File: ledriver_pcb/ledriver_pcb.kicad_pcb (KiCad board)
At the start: 2 copper layers, 83.8 x 73.7 mm, 43 parts, among them J1 5-12vdc, J10 POT2, J11 I2C, J12 Serial2, J13 Serial1, J14 M3, J15 M3, J16 M3, J17 M3, J2 USB_B, J3 USB+-, J4 USB_EXT, J5 RJ2, J6 CONN-114-00841-68-MICROSD, J7 RJ1, J8 led_out_clk, J9 POT1, SW1 SW_SPST, SW2 SW_SPST, SW3 SW_SPST, U1 L7805, U2 MCP1825, U3 WIZ820IO, U4 74HC245, U5 Teensy3.2

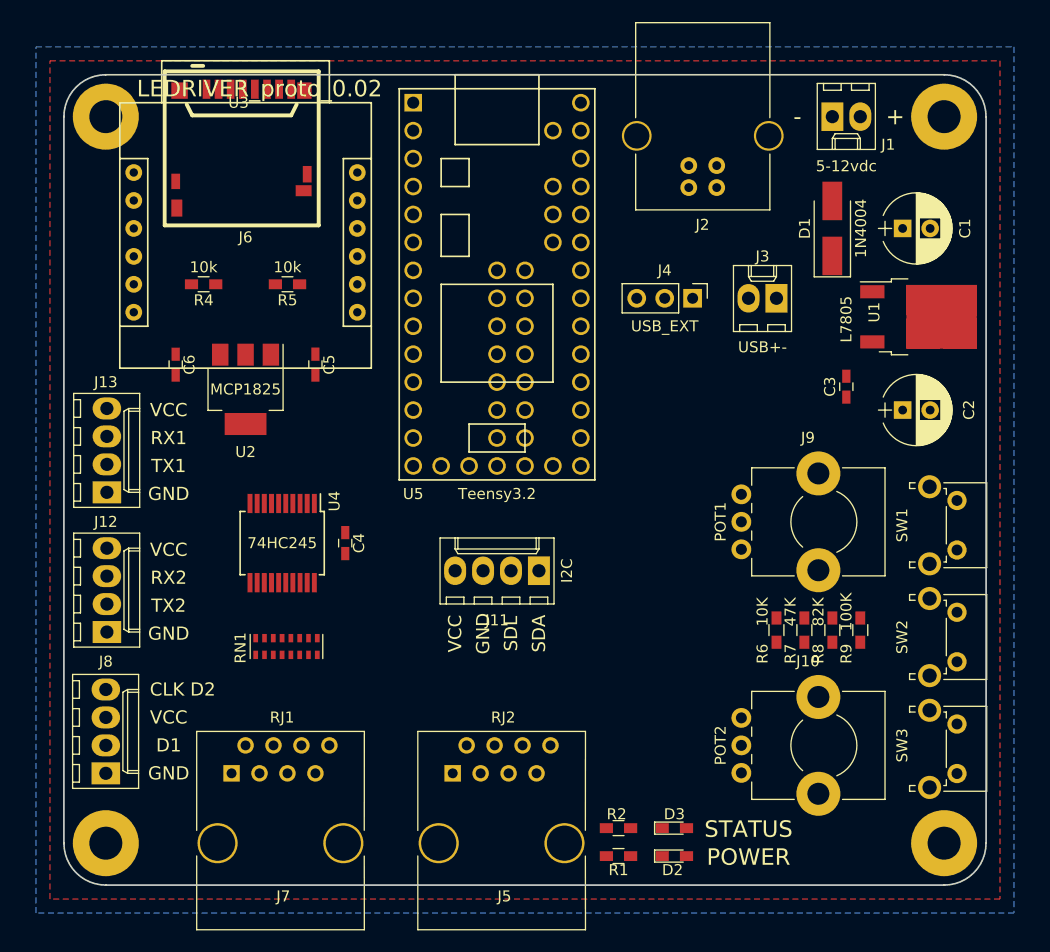
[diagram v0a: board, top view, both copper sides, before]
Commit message: changed led SPI output to use pin 7 and 14, not reflected in layout
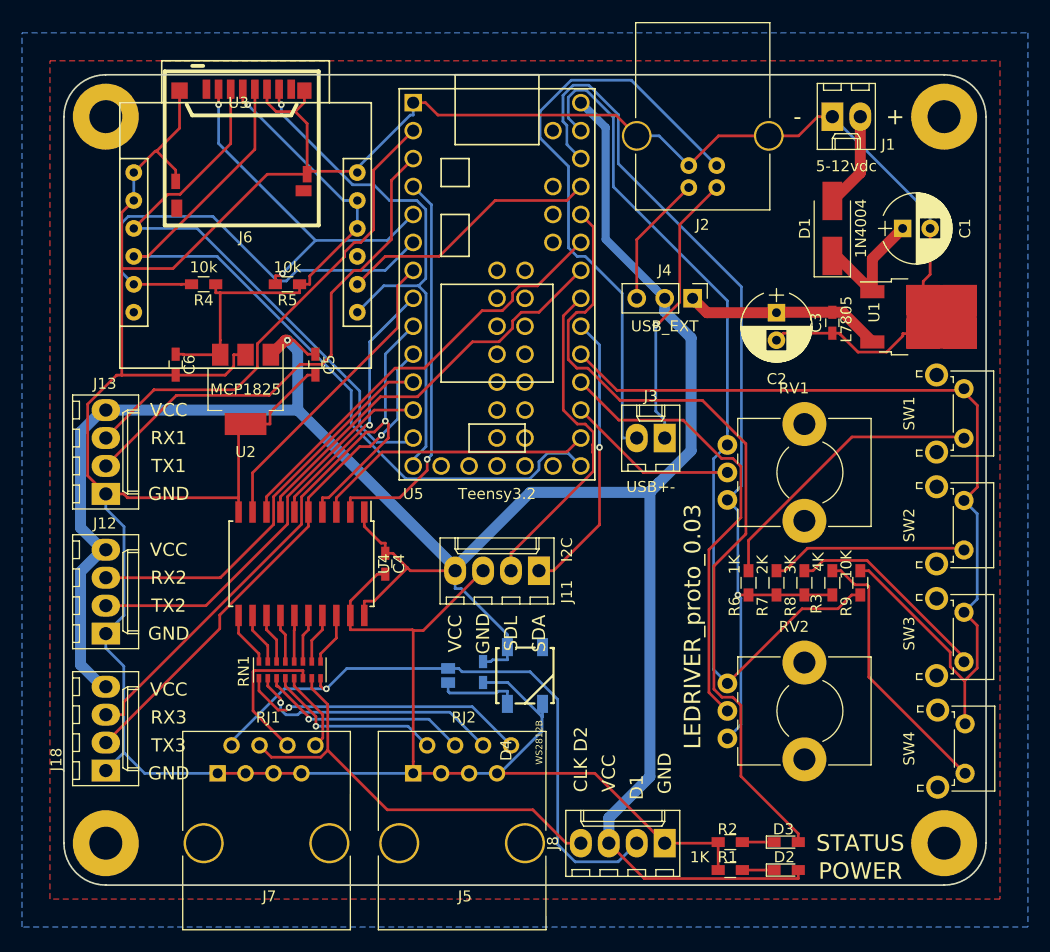
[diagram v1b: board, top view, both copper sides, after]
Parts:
- removed J10: POT2, Potentiometers:Potentiometer_Bourns_PTV09A-1_Horizontal
- removed J9: POT1, Potentiometers:Potentiometer_Bourns_PTV09A-1_Horizontal
- added C7: C, Capacitors_SMD:C_0603_HandSoldering, B.Cu at (138.4, 88.6)
- added D4: WS2812B, SparkFun-LED:WS2812B, B.Cu at (142.2, 88.9)
- added J18: Serial3, Connectors_Molex:Molex_KK-6410-04_04x2.54mm_Straight, F.Cu at (104.1, 97.5)
- added J19: underglow, Connectors:GS2, B.Cu at (135.3, 88.9)
- added R3: 4K, Resistors_SMD:R_0603_HandSoldering, F.Cu at (170.2, 80.5)
- added RV1: POT, Potentiometers:Potentiometer_Bourns_PTV09A-1_Horizontal, F.Cu at (160.6, 72.9)
- added RV2: POT, Potentiometers:Potentiometer_Bourns_PTV09A-1_Horizontal, F.Cu at (160.6, 94.6)
- added SW4: SW_SPST, Buttons_Switches_THT:SW_Tactile_SPST_Angled_PTS645Vx39-2LFS, F.Cu at (182.2, 93.3)
- R6: value 10K -> 1K
- R7: value 47K -> 2K
- R8: value 82K -> 3K
- R9: value 100K -> 10K
- U4: footprint Housings_SSOP:SSOP-20_5.3x7.2mm_Pitch0.65mm -> Housings_SOIC:SOIC-20W_7.5x12.8mm_Pitch1.27mm
- moved J8 51.2 mm to (154.9, 104.1), turned to 180 degrees
- moved J3 16.3 mm to (154.9, 67.3)
- moved C2 14.5 mm to (165.1, 55.9), turned to 270 degrees
- moved D2 10.2 mm to (166.0, 106.6)
- moved D3 10.2 mm to (166.0, 104.0)
- moved R1 10.2 mm to (160.9, 106.6)
- moved R2 10.2 mm to (160.9, 104.0)
- moved SW2 10.2 mm to (182.1, 73.0)
- moved SW1 10.2 mm to (182.1, 62.8)
- moved SW3 10.2 mm to (182.1, 83.2)
- moved C3 5.95 mm to (170.2, 56.8)
- moved R8 4.99 mm to (167.6, 80.5)
- moved R6 4.99 mm to (162.6, 80.5)
- moved R7 4.99 mm to (165.1, 80.5)
- moved R9 4.30 mm to (172.7, 80.5)
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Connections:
- R6 pad 1: VCC -> +3V3
- R7 pad 1: VCC -> +3V3
- R8 pad 1: VCC -> +3V3
- R9 pad 1: GND -> GNDA
- U5 pad 31: (no net) -> +3V3
- U5 pad 32: (no net) -> GNDA
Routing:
- net GND: track 0.00 -> 357.4 mm
- net VCC: track 0.00 -> 225.8 mm, vias 0 -> 1
- net +3V3: track 0.00 -> 84.4 mm, vias 0 -> 1
- net /BUTTONS: track 0.00 -> 84.0 mm
- net GNDA: track 0.00 -> 81.1 mm
- net /STATUS: track 0.00 -> 75.5 mm
- net /SPI_SCK: track 0.00 -> 73.2 mm
- net /DATA_3_PIN_7: track 0.00 -> 59.5 mm, vias 0 -> 1
- net Net-(J19-Pad2): track 0.00 -> 57.0 mm, vias 0 -> 1
- net Net-(J2-Pad3): track 0.00 -> 55.0 mm
- net /SPI_DOUT: track 0.00 -> 52.4 mm
- net /SPI_DIN: track 0.00 -> 49.9 mm, vias 0 -> 1
- net /DATA_4_PIN_8: track 0.00 -> 47.4 mm, vias 0 -> 1
- net /TX1: track 0.00 -> 46.0 mm
- net Net-(C6-Pad1): track 0.00 -> 44.5 mm, vias 0 -> 1
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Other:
- board text added: "LEDRIVER_proto_0.03"
- board text added: "RX3"
- board text added: "TX3"
- board text removed: "LEDRIVER_proto_0.02"
- board text removed: "sdcard move up"

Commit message: hjaha
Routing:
- net GND: track 357.4 -> 0.00 mm
- net VCC: track 225.8 -> 0.00 mm, vias 1 -> 0
- net +3V3: track 84.4 -> 0.00 mm, vias 1 -> 0
- net /BUTTONS: track 84.0 -> 0.00 mm
- net GNDA: track 81.1 -> 0.00 mm
- net /STATUS: track 75.5 -> 0.00 mm
- net /SPI_SCK: track 73.2 -> 0.00 mm
- net /DATA_3_PIN_7: track 59.5 -> 0.00 mm, vias 1 -> 0
- net Net-(J19-Pad2): track 57.0 -> 0.00 mm, vias 1 -> 0
- net Net-(J2-Pad3): track 55.0 -> 0.00 mm
- net /SPI_DOUT: track 52.4 -> 0.00 mm
- net /SPI_DIN: track 49.9 -> 0.00 mm, vias 1 -> 0
- net /DATA_4_PIN_8: track 47.4 -> 0.00 mm, vias 1 -> 0
- net /TX1: track 46.0 -> 0.00 mm
- net Net-(C6-Pad1): track 44.5 -> 0.00 mm, vias 1 -> 0
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- removed copper zone on B.Cu, net GND
- removed copper zone on F.Cu, net GND

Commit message: wip
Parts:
- added REF**: Pin_Header_Straight_1x01_Pitch2.00mm, Pin_Headers:Pin_Header_Straight_1x01_Pitch2.00mm, F.Cu at (168.2, 70.4)
- added REF**: Pin_Header_Straight_1x01_Pitch2.00mm, Pin_Headers:Pin_Header_Straight_1x01_Pitch2.00mm, F.Cu at (168.2, 92.1)
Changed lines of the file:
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@@
 (kicad_pcb (version 4) (host pcbnew 4.0.7-e2-6376~58~ubuntu16.04.1)
   (general
-    (links 143)
-    (no_connects 102)
+    (links 0)
+    (no_connects 139)
     (area 100.254999 34.214999 184.225001 108.025001)
     (thickness 1.6)
@@
     (tracks 0)
     (zones 0)
-    (modules 49)
+    (modules 51)
     (nets 59)
   )
@@
   )
   (setup
-    (last_trace_width 0.5)
+    (last_trace_width 0.25)
     (user_trace_width 0.3)
     (user_trace_width 0.5)
@@
     (add_net "Net-(RN1-Pad8)")
     (add_net VCC)
+  )
+  (module Pin_Headers:Pin_Header_Straight_1x01_Pitch2.00mm (layer F.Cu)
+    (at 168.15 70.375)
+    (descr "Through hole straight pin header, 1x01, 2.00mm pitch, single row")
+    (tags "Through hole pin header THT 1x01 2.00mm single row")
+    (fp_text reference REF** (at 0 -2.06) (layer F.SilkS)
+      (effects (font (size 1 1) (thickness 0.15)))
+    )
+    (fp_text value Pin_Header_Straight_1x01_Pitch2.00mm (at 0 2.06) (layer F.Fab)
+      (effects (font (size 1 1) (thickness 0.15)))
+    )
+    (fp_line (start -0.5 -1) (end 1 -1) (layer F.Fab) (width 0.1))
+    (fp_line (start 1 -1) (end 1 1) (layer F.Fab) (width 0.1))
+    (fp_line (start 1 1) (end -1 1) (layer F.Fab) (width 0.1))
+    (fp_line (start -1 1) (end -1 -0.5) (layer F.Fab) (width 0.1))
+    (fp_line (start -1 -0.5) (end -0.5 -1) (layer F.Fab) (width 0.1))
+    (fp_line (start -1.06 1.06) (end 1.06 1.06) (layer F.SilkS) (width 0.12))
+    (fp_line (start -1.06 1) (end -1.06 1.06) (layer F.SilkS) (width 0.12))
+    (fp_line (start 1.06 1) (end 1.06 1.06) (layer F.SilkS) (width 0.12))
+    (fp_line (start -1.06 1) (end 1.06 1) (layer F.SilkS) (width 0.12))
+    (fp_line (start -1.06 0) (end -1.06 -1.06) (layer F.SilkS) (width 0.12))
+    (fp_line (start -1.06 -1.06) (end 0 -1.06) (layer F.SilkS) (width 0.12))
+    (fp_line (start -1.5 -1.5) (end -1.5 1.5) (layer F.CrtYd) (width 0.05))
+    (fp_line (start -1.5 1.5) (end 1.5 1.5) (layer F.CrtYd) (width 0.05))
+    (fp_line (start 1.5 1.5) (end 1.5 -1.5) (layer F.CrtYd) (width 0.05))
+    (fp_line (start 1.5 -1.5) (end -1.5 -1.5) (layer F.CrtYd) (width 0.05))
+    (fp_text user %R (at 0 0 90) (layer F.Fab)
+      (effects (font (size 1 1) (thickness 0.15)))
+    )
+    (pad 1 thru_hole rect (at 0 0) (size 1.35 1.35) (drill 0.8) (layers *.Cu *.Mask))
+    (model ${KISYS3DMOD}/Pin_Headers.3dshapes/Pin_Header_Straight_1x01_Pitch2.00mm.wrl
+      (at (xyz 0 0 0))
+      (scale (xyz 1 1 1))
+      (rotate (xyz 0 0 0))
+    )
   )
   (module Capacitors_THT:CP_Radial_D6.3mm_P2.50mm (layer F.Cu)
@@
       (rotate (xyz 0 0 0))
     )
+  )
+  (module Pin_Headers:Pin_Header_Straight_1x01_Pitch2.00mm (layer F.Cu)
+    (at 168.15 92.125)
+    (descr "Through hole straight pin header, 1x01, 2.00mm pitch, single row")
+    (tags "Through hole pin header THT 1x01 2.00mm single row")
+    (fp_text reference REF** (at 0 -2.06) (layer F.SilkS)
+      (effects (font (size 1 1) (thickness 0.15)))
+    )
+    (fp_text value Pin_Header_Straight_1x01_Pitch2.00mm (at 0 2.06) (layer F.Fab)
+      (effects (font (size 1 1) (thickness 0.15)))
+    )
+    (fp_line (start -0.5 -1) (end 1 -1) (layer F.Fab) (width 0.1))
+    (fp_line (start 1 -1) (end 1 1) (layer F.Fab) (width 0.1))
+    (fp_line (start 1 1) (end -1 1) (layer F.Fab) (width 0.1))
+    (fp_line (start -1 1) (end -1 -0.5) (layer F.Fab) (width 0.1))
+    (fp_line (start -1 -0.5) (end -0.5 -1) (layer F.Fab) (width 0.1))
+    (fp_line (start -1.06 1.06) (end 1.06 1.06) (layer F.SilkS) (width 0.12))
+    (fp_line (start -1.06 1) (end -1.06 1.06) (layer F.SilkS) (width 0.12))
+    (fp_line (start 1.06 1) (end 1.06 1.06) (layer F.SilkS) (width 0.12))
+    (fp_line (start -1.06 1) (end 1.06 1) (layer F.SilkS) (width 0.12))
+    (fp_line (start -1.06 0) (end -1.06 -1.06) (layer F.SilkS) (width 0.12))
+    (fp_line (start -1.06 -1.06) (end 0 -1.06) (layer F.SilkS) (width 0.12))
+    (fp_line (start -1.5 -1.5) (end -1.5 1.5) (layer F.CrtYd) (width 0.05))
+    (fp_line (start -1.5 1.5) (end 1.5 1.5) (layer F.CrtYd) (width 0.05))
+    (fp_line (start 1.5 1.5) (end 1.5 -1.5) (layer F.CrtYd) (width 0.05))
+    (fp_line (start 1.5 -1.5) (end -1.5 -1.5) (layer F.CrtYd) (width 0.05))
+    (fp_text user %R (at 0 0 90) (layer F.Fab)
+      (effects (font (size 1 1) (thickness 0.15)))
+    )
+    (pad 1 thru_hole rect (at 0 0) (size 1.35 1.35) (drill 0.8) (layers *.Cu *.Mask))
+    (model ${KISYS3DMOD}/Pin_Headers.3dshapes/Pin_Header_Straight_1x01_Pitch2.00mm.wrl
+      (at (xyz 0 0 0))
+      (scale (xyz 1 1 1))
+      (rotate (xyz 0 0 0))
+    )
